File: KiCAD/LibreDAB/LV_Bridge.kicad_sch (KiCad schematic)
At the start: 35 parts, among them J1 TS30050050-040, J2 TS30050050-040, J3 TS30050050-040, J4 TS30050050-040, J5 PZ254VS-11-03P-B01, J6 PZ254VS-11-03P-B01, J7 PZ254VS-11-03P-B01, Q1 SP010N01BGHTO, Q2 SP010N01BGHTO, Q3 SP010N01BGHTO, Q4 SP010N01BGHTO

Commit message: Added more gate drive schematic info
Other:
- sheet Gate_Driver ports: added MID, PWM-H, PWM-L, QH-G, QL-G; removed none
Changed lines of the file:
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@@
+			)
+		)
+		(pin "MID" bidirectional
+			(at 196.85 30.48 0)
+			(effects
+				(font
+					(size 1.27 1.27)
+				)
+				(justify right)
+			)
+		)
+		(pin "PWM-H" input
+			(at 166.37 36.83 180)
+			(effects
+				(font
+					(size 1.27 1.27)
+				)
+				(justify left)
+			)
+		)
+		(pin "PWM-L" input
+			(at 166.37 40.64 180)
+			(effects
+				(font
+					(size 1.27 1.27)
+				)
+				(justify left)
+			)
+		)
+		(pin "QH-G" output
+			(at 196.85 26.67 0)
+			(effects
+				(font
+					(size 1.27 1.27)
+				)
+				(justify right)
+			)
+		)
+		(pin "QL-G" bidirectional
+			(at 196.85 34.29 0)
+			(effects
+				(font
+					(size 1.27 1.27)
+				)
+				(justify right)
 			)
 		)

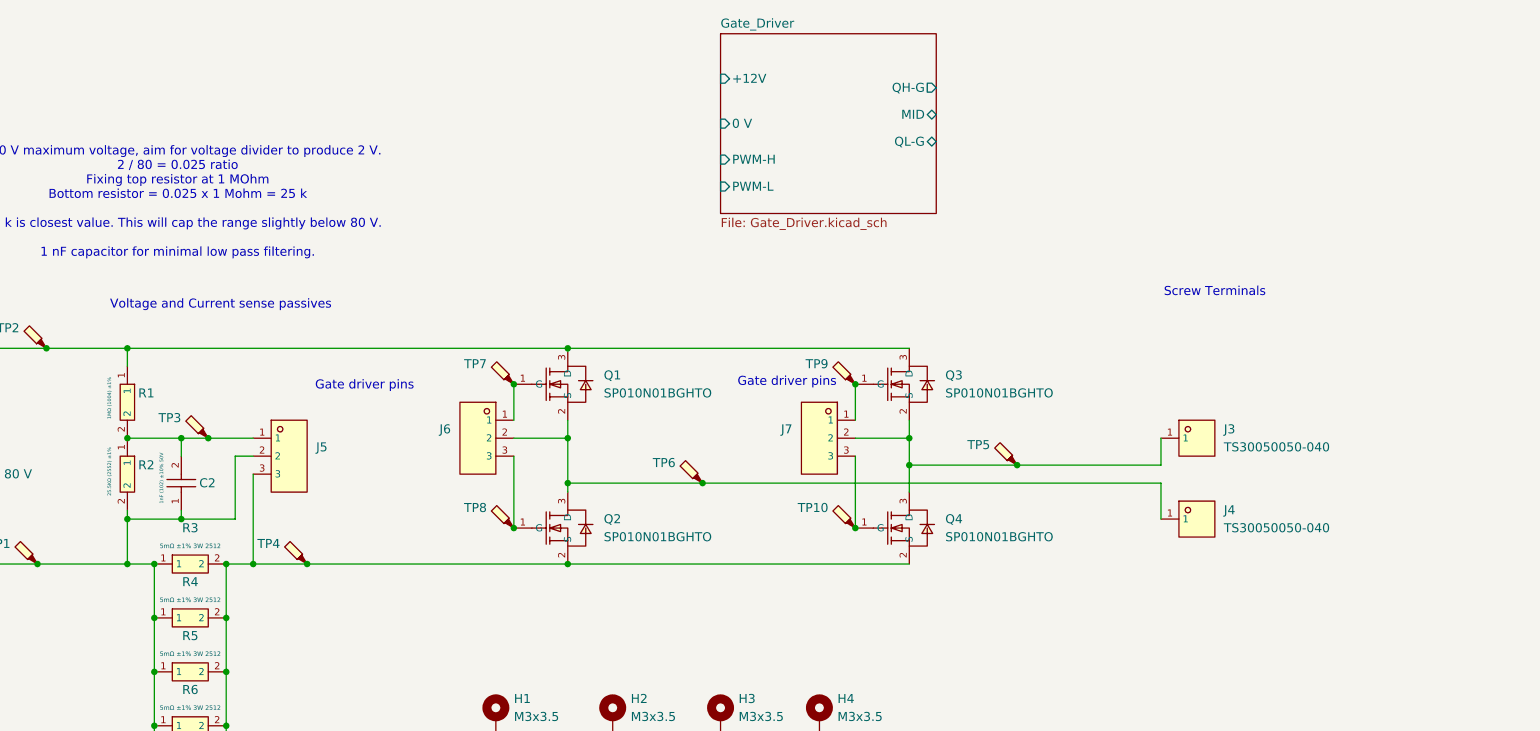
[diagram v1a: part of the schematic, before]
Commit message: Gate Drive schematic and footprints added
This is the last commit before trying the combined gate drive and sensing on the power board.
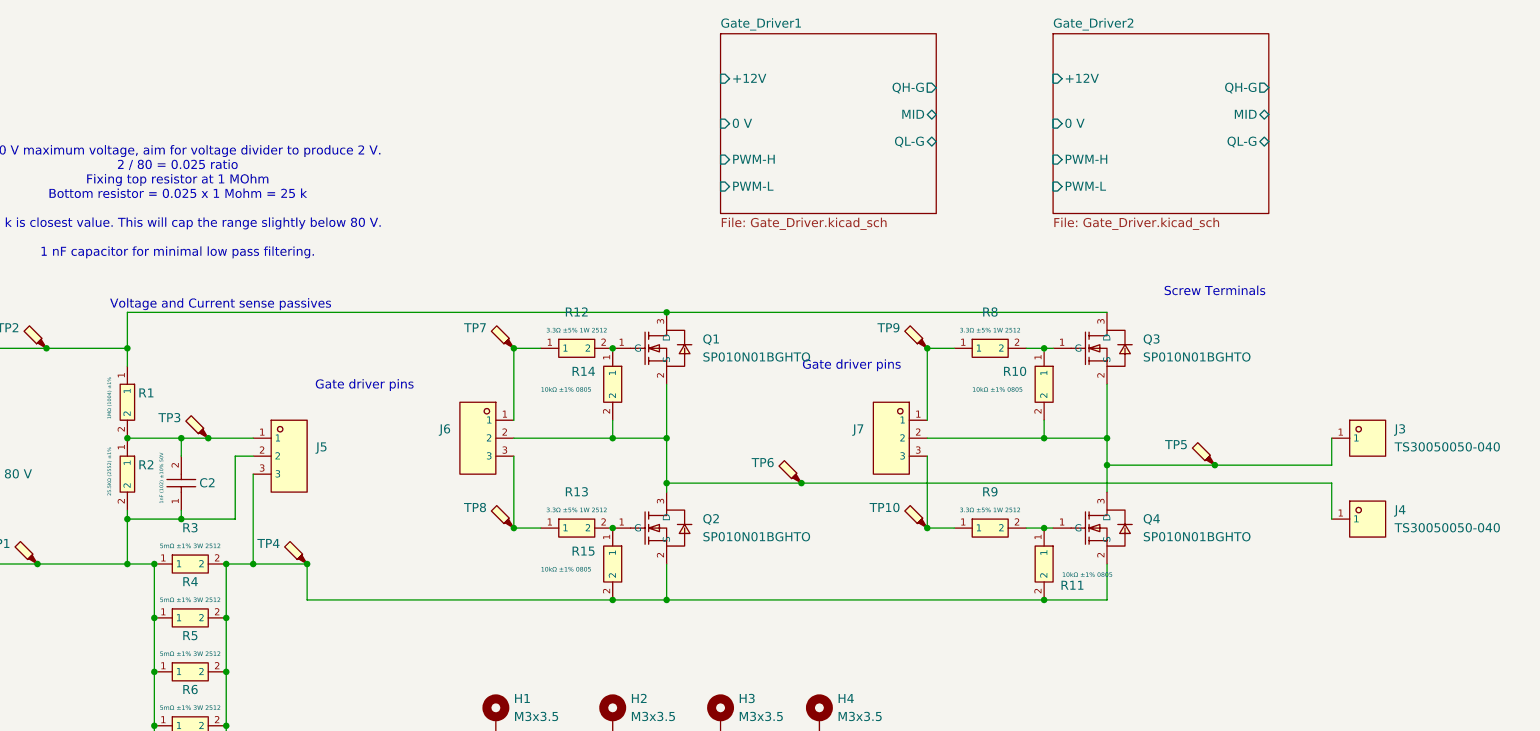
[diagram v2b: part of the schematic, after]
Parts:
- added R10, R11, R14, R15: 10kΩ ±1% 0805, lcsc_footprints:C2907219_R0805, symbol lcsc_imported:RES 10kΩ ±1% 125mW 0805
- added R12, R13, R8, R9: 3.3Ω ±5% 1W 2512, lcsc_footprints:C393074_RES-SMD_L6_4-W3_2-1, symbol lcsc_imported:1W_3.3Ω_200V_Thick_Film_Resistor_±400ppm/℃_±5%_2512_Chip_Resistor
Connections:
- net at J4.1, J6.2, Q1.2 (S)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: now also R14.2
- net at J7.1, TP9.1: now also R8.1; no longer Q3.1 (G)
- net at J5.3, Q2.2 (S), Q4.2 (S)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: now also R11.2, R15.2
- net at J6.1, TP7.1: now also R12.1; no longer Q1.1 (G)
- net at J3.1, J7.2, Q3.2 (S)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: now also R10.2
- net at J6.3, TP8.1: now also R13.1; no longer Q2.1 (G)
- net at J7.3, TP10.1: now also R9.1; no longer Q4.1 (G)
- new net: Q1.1 (G), R12.2, R14.1
- new net: Q2.1 (G), R13.2, R15.1
- new net: Q3.1 (G), R10.1, R8.2
- new net: Q4.1 (G), R11.1, R9.2
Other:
- sheet Gate_Driver renamed Gate_Driver1
- added sheet Gate_Driver2 (Gate_Driver.kicad_sch)
- moved on the sheet: J3, J4, J7, Q1, Q2, Q3, Q4, TP10, TP5, TP6, TP7, TP9

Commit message: Edits to gate drive circuitry
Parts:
- removed J6, J7: PZ254VS-11-03P-B01, lcsc_footprints:C41432921_HDR-SMD_3P-P2_54-V-M-LS4_8_R2, symbol lcsc_imported:PZ254VS-11-03P-B01
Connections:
- net LSW1: now reaches J4.1, Q1.2 (S), Q2.3 (D), R14.2, TP6.1
- net HO2: now reaches R8.1, TP9.1
- net LO1: now reaches R13.1, TP8.1
- net HO1: now reaches R12.1, TP7.1
- net LSW2: now reaches J3.1, Q3.2 (S), Q4.3 (D), R10.2, TP5.1
- net LO2: now reaches R9.1, TP10.1

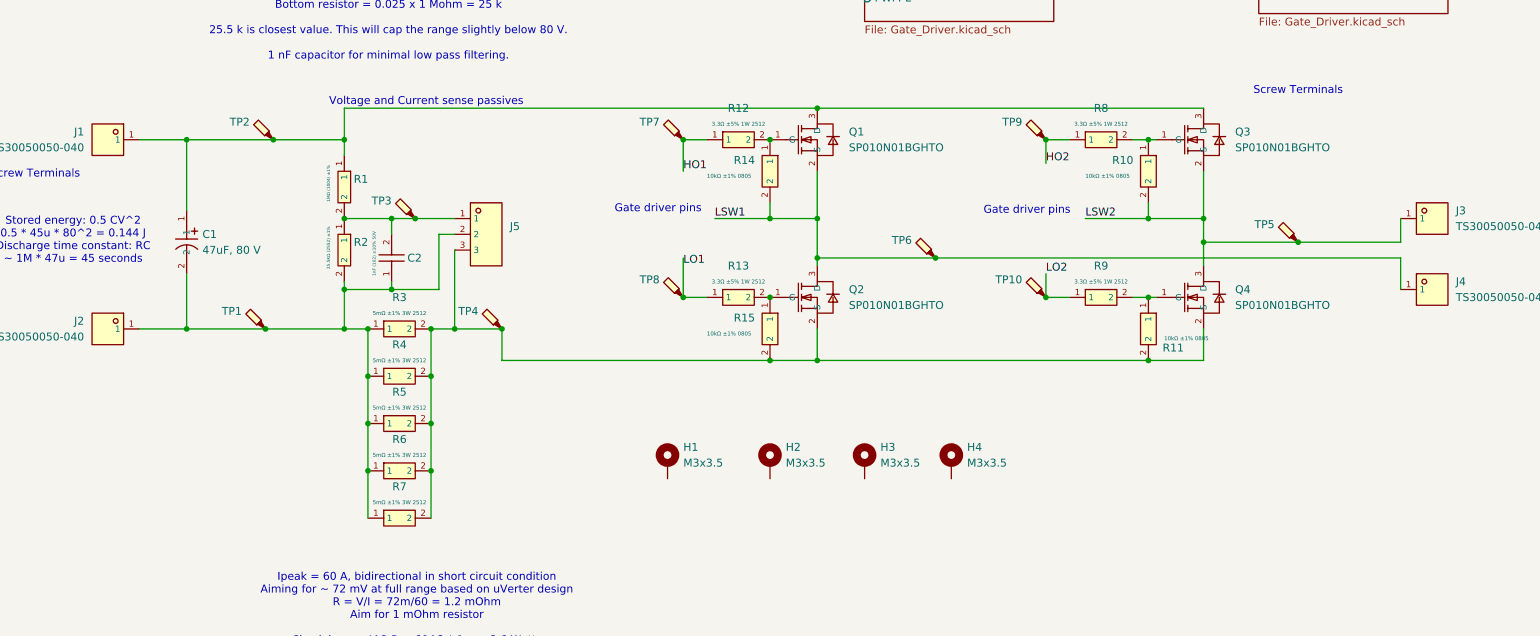
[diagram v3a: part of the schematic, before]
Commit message: Tidied symbols
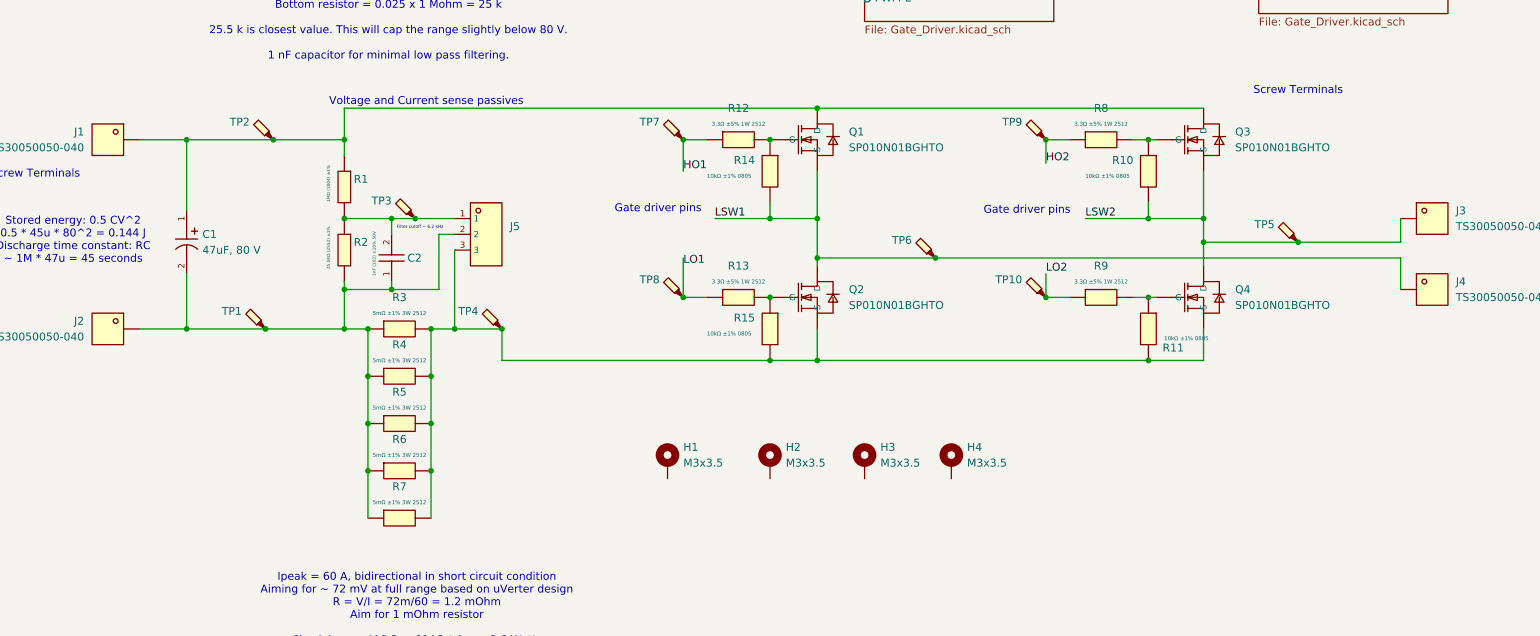
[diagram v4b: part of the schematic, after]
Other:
- note added: "Filter cutoff ~ 6.2 kHz"
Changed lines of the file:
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@@
+		)
+	)
+	(text "Filter cutoff ~ 6.2 kHz"
+		(exclude_from_sim no)
+		(at 94.742 77.724 0)
+		(effects
+			(font
+				(size 0.5 0.5)
+			)
 		)
 	)

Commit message: Minor edits
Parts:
- removed J5: PZ254VS-11-03P-B01, lcsc_footprints:C41432921_HDR-SMD_3P-P2_54-V-M-LS4_8_R2, symbol lcsc_imported:PZ254VS-11-03P-B01
- added U3, U4: MCP6486UT-E/LT, lcsc_footprints:C5224800_SC-70-5_L2_1-W1_3-P0_65-LS2_3-BL, symbol lcsc_imported:MCP6486UT-E/LT
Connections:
- net V_LV+: now reaches C1.1, J1.1, Q1.3 (D), Q3.3 (D), R1.1, TP2.1
- net V_LV_Divider: now reaches C2.2, R1.2, R2.1, TP3.1
- net V_LV_Divider: now also U3.1 (IN+)
- net V_LV-: now reaches C1.2, C2.1, J2.1, R2.2, R3.1, R4.1, R5.1, R6.1, R7.1, TP1.1
- net V_LV-: now also U4.3 (IN-), U4.4 (OUT)
- net GND: now reaches Q2.2 (S), Q4.2 (S), R11.2, R15.2, R3.2, R4.2, R5.2, R6.2, R7.2, TP4.1
- new net: U3.3 (IN-), U3.4 (OUT)
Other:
- note added: "1.024 V reference for measurement offset"
- note added: "Voltage Sense buffer"

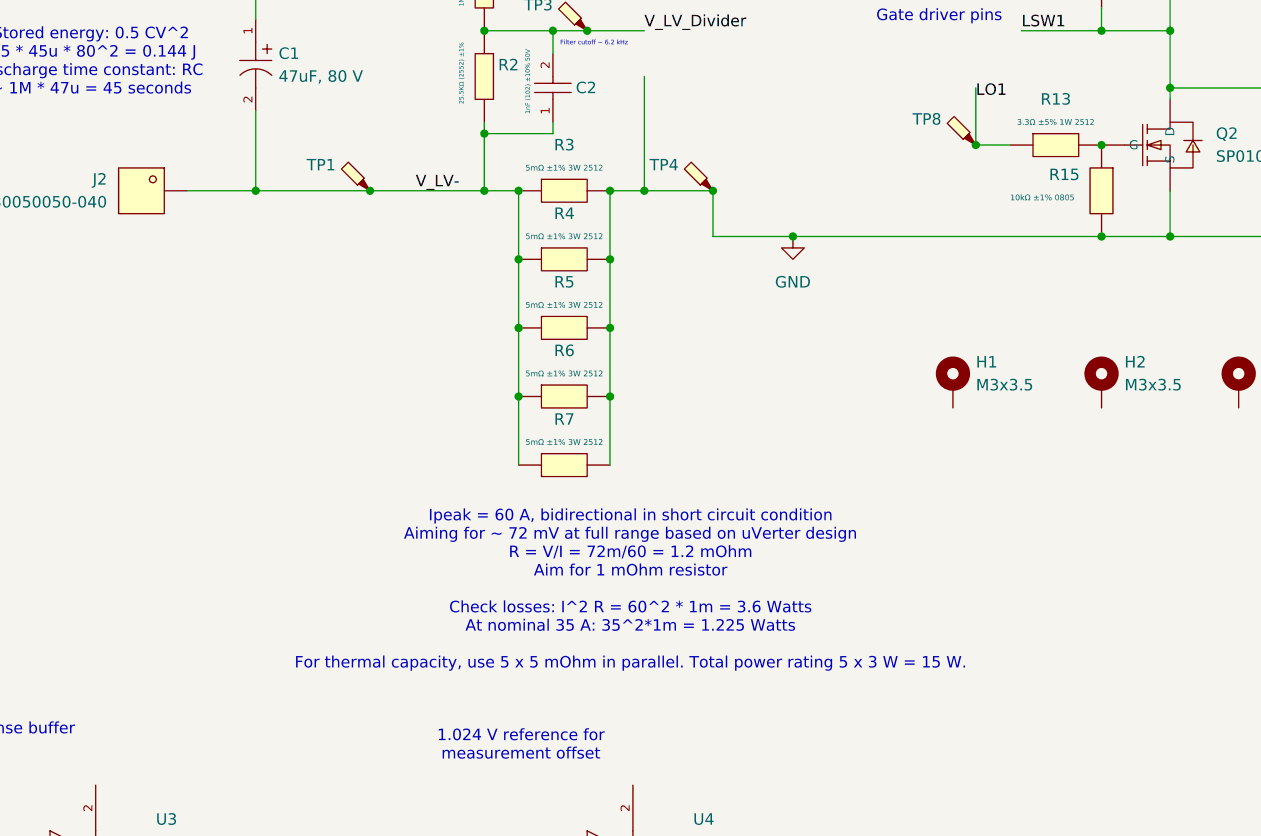
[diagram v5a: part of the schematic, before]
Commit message: Added multi-pad current sense resistor footprint
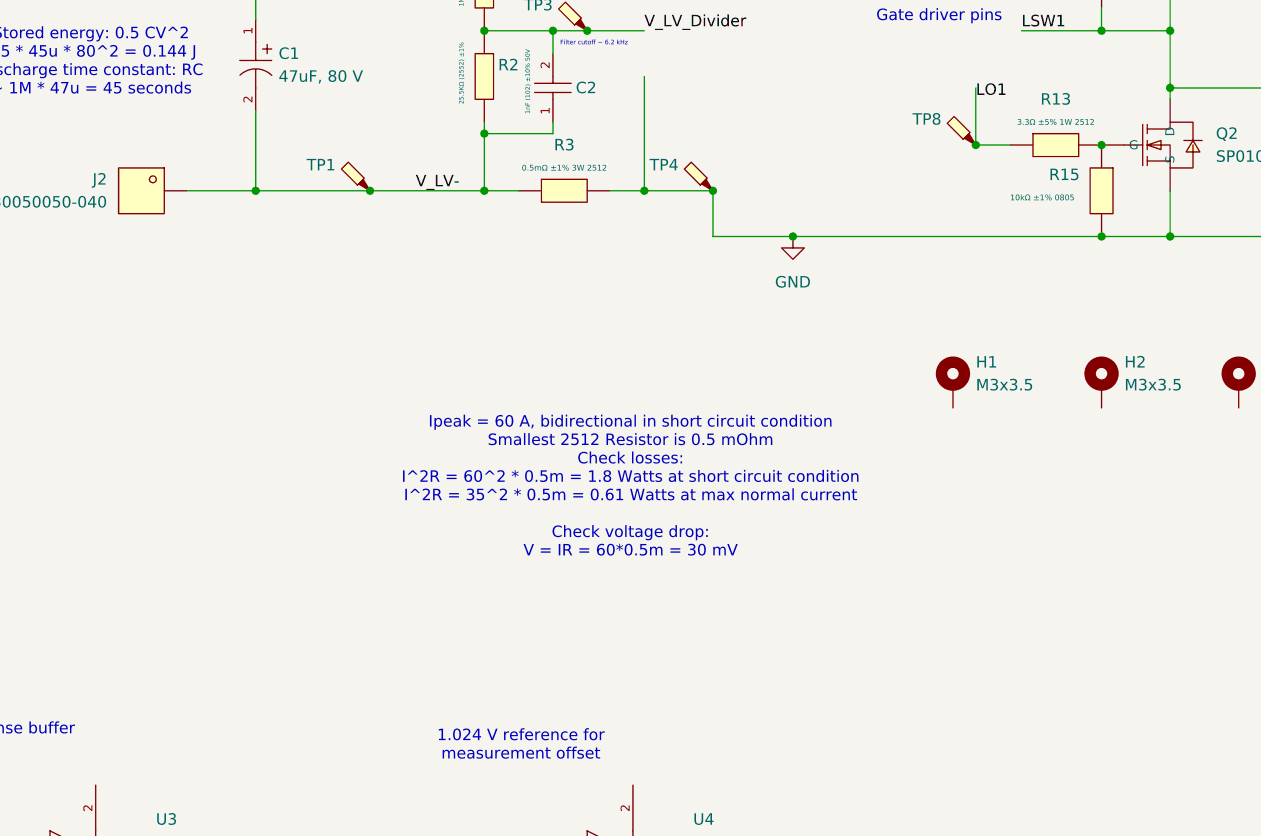
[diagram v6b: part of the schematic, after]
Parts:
- removed R3, R4, R5, R6, R7: 5mΩ ±1% 3W 2512, lcsc_footprints:C393074_RES-SMD_L6_4-W3_2-1, symbol lcsc_imported:RLP25FEGMR005
- added R3: 0.5mΩ ±1% 3W 2512, lcsc_footprints:C710260_RES-SMD_L6_4-W3_2_RLM25, symbol lcsc_imported:0.5mΩ ±1% 3W 2512
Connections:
- net GND: now also R3.2
- net V_LV-: now also R3.1
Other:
- note added: "Ipeak = 60 A, bidirectional in short circuit condition Smallest 2512 Resistor is 0.5 mOhm Check losses: I^2R = 60^2 * 0.5m = 1.8 Watts at short circuit condition I^2R = 35^2 * 0.5m = 0.61 Watts at max normal current Check voltage drop: V = IR = 60*0.5m = 30 mV"
- note removed: "Ipeak = 60 A, bidirectional in short circuit condition Aiming for ~ 72 mV at full range based on uVerter design R = V/I = 72m/60 = 1.2 mOhm Aim for 1 mOhm resistor Check losses: I^2 R = 60^2 * 1m = 3.6 Watts At nominal 35 A: 35^2*1m = 1.225 Watts For thermal capacity, use 5 x 5 mOhm in parallel. Total power rating 5 x 3 W = 15 W."
